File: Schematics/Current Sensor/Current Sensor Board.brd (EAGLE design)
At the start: 67 x 29.2 mm, 4 parts

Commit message: added berbers for current sensor board and flowchart
flow chart is for the main control program.
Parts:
- added C1: (no value), rcl:C050-050X075
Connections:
- net GND: now also C1.2
- net N$3: now also C1.1
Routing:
- net N$3: track 27.1 -> 30.1 mm
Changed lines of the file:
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@@
 <element name="U$3" library="Headers" package="1X2_100MIL" value="1X2HEADER_100MIL" x="2.54" y="15.24" rot="R270"/>
 <element name="IC1" library="v-reg" package="78XXS" value="" x="12.7" y="16.51" rot="R270"/>
+<element name="C1" library="rcl" package="C050-050X075" value="" x="50.8" y="27.94" rot="R180"/>
 </elements>
 <signals>
@@
 <vertex x="0" y="2.54"/>
 </polygon>
+<contactref element="C1" pad="2"/>
 </signal>
 <signal name="N$3">
@@
 <wire x1="44.45" y1="15.24" x2="54.61" y2="25.4" width="0.4064" layer="16"/>
 <wire x1="54.61" y1="25.4" x2="62.23" y2="25.4" width="0.4064" layer="16"/>
+<contactref element="C1" pad="1"/>
+<wire x1="53.34" y1="27.94" x2="53.34" y2="26.67" width="0.4064" layer="16"/>
+<wire x1="53.34" y1="26.67" x2="54.61" y2="25.4" width="0.4064" layer="16"/>
 </signal>
 <signal name="N$1">

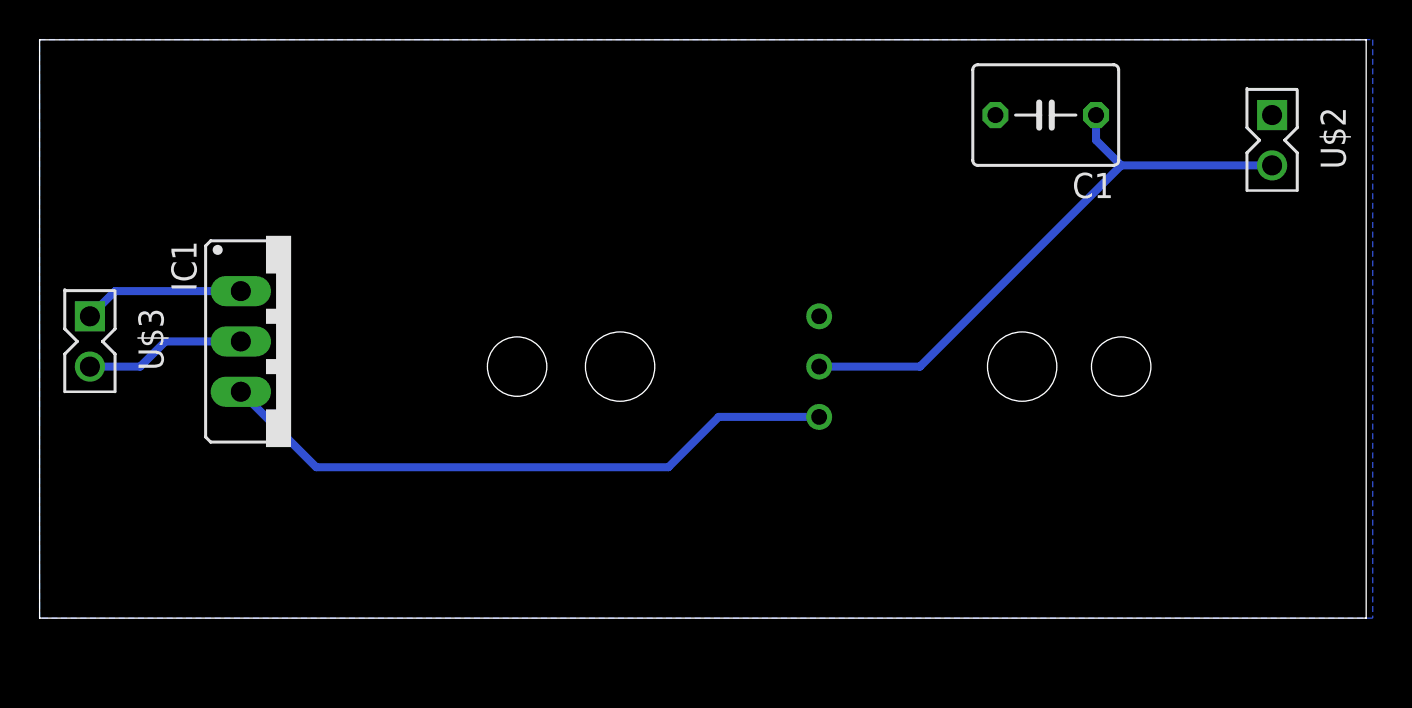
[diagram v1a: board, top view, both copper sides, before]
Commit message: updated documentation and scheamtics
updated current sensor board, and added manual for stepper motor
controller
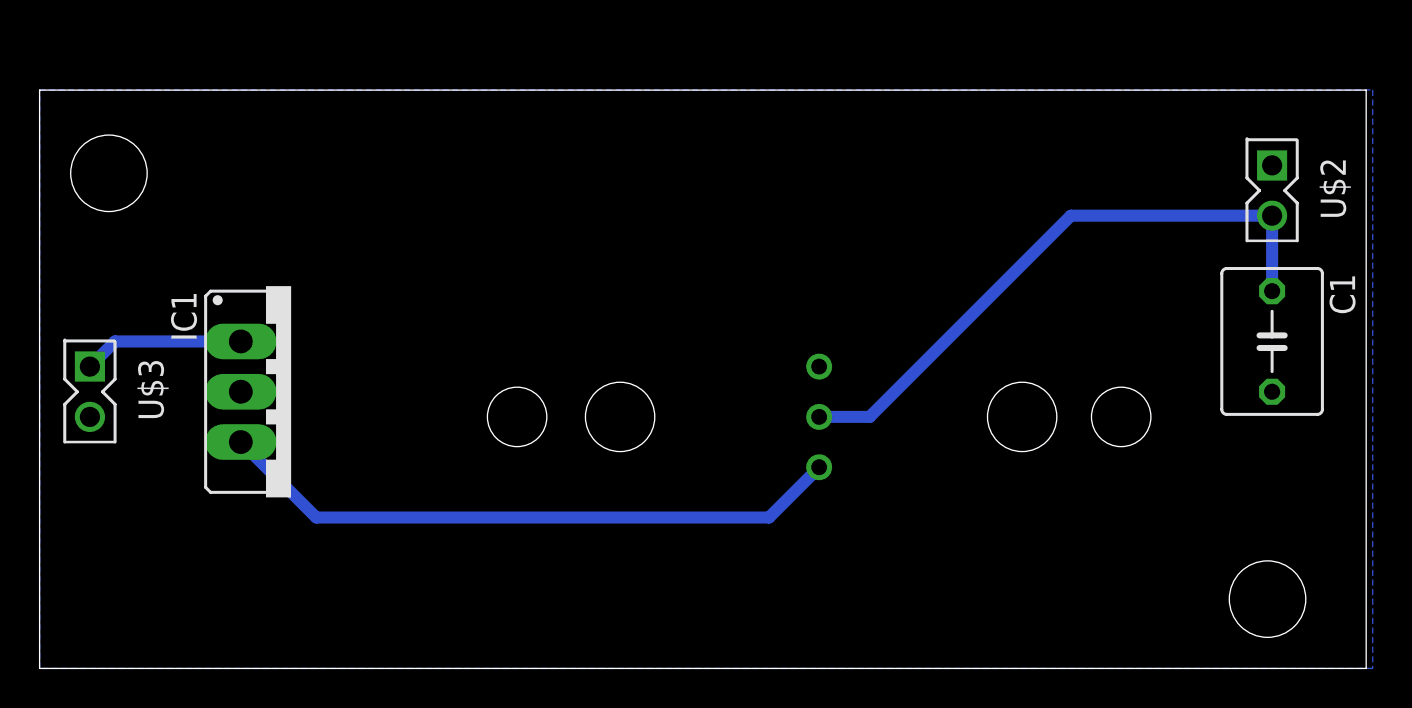
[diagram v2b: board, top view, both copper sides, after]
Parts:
- moved C1 16.2 mm to (62.2, 16.5), turned to 270 degrees
- moved IC1 2.54 mm to (12.7, 14.0)
- moved U$1 2.54 mm to (54.6, 12.7)
- moved U$3 2.54 mm to (2.54, 12.7)
- moved U$2 2.54 mm to (62.2, 22.9)
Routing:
- net GND: track 8.15 -> 0.00 mm
- net N$3: track 30.1 -> 30.9 mm
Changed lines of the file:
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@@
 <setting verticaltext="up"/>
 </settings>
-<grid distance="0.05" unitdist="inch" unit="inch" style="lines" multiple="1" display="yes" altdistance="0.025" altunitdist="inch" altunit="inch"/>
+<grid distance="0.05" unitdist="inch" unit="mil" style="lines" multiple="1" display="yes" altdistance="0.025" altunitdist="inch" altunit="inch"/>
 <layers>
 <layer number="1" name="Top" color="4" fill="1" visible="yes" active="yes"/>
@@
 <layer number="43" name="vRestrict" color="2" fill="10" visible="yes" active="yes"/>
 <layer number="44" name="Drills" color="7" fill="1" visible="no" active="yes"/>
-<layer number="45" name="Holes" color="7" fill="1" visible="no" active="yes"/>
+<layer number="45" name="Holes" color="7" fill="1" visible="yes" active="yes"/>
 <layer number="46" name="Milling" color="3" fill="1" visible="no" active="yes"/>
 <layer number="47" name="Measures" color="7" fill="1" visible="no" active="yes"/>
@@
 <board>
 <plain>
-<wire x1="0" y1="2.54" x2="66.98" y2="2.54" width="0" layer="20"/>
-<wire x1="66.98" y1="2.54" x2="66.98" y2="31.74" width="0" layer="20"/>
-<wire x1="66.98" y1="31.74" x2="0" y2="31.74" width="0" layer="20"/>
-<wire x1="0" y1="31.74" x2="0" y2="2.54" width="0" layer="20"/>
+<wire x1="0" y1="0" x2="66.98" y2="0" width="0" layer="20"/>
+<wire x1="66.98" y1="0" x2="66.98" y2="29.2" width="0" layer="20"/>
+<wire x1="66.98" y1="29.2" x2="0" y2="29.2" width="0" layer="20"/>
+<wire x1="0" y1="29.2" x2="0" y2="0" width="0" layer="20"/>
+<hole x="3.5" y="25" drill="3.8608"/>
+<hole x="62" y="3.5" drill="3.8608"/>
 </plain>
 <attributes>
@@
 </autorouter>
 <elements>
-<element name="U$1" library="Current Sensors" package="CSLA1DJ" value="CSLA1DJ" x="54.61" y="15.24" rot="R180"/>
-<element name="U$2" library="Headers" package="1X2_100MIL" value="1X2HEADER_100MIL" x="62.23" y="25.4" rot="R270"/>
-<element name="U$3" library="Headers" package="1X2_100MIL" value="1X2HEADER_100MIL" x="2.54" y="15.24" rot="R270"/>
-<element name="IC1" library="v-reg" package="78XXS" value="" x="12.7" y="16.51" rot="R270"/>
-<element name="C1" library="rcl" package="C050-050X075" value="" x="50.8" y="27.94" rot="R180"/>
+<element name="U$1" library="Current Sensors" package="CSLA1DJ" value="CSLA1DJ" x="54.61" y="12.7" rot="R180"/>
+<element name="U$2" library="Headers" package="1X2_100MIL" value="1X2HEADER_100MIL" x="62.23" y="22.86" rot="R270"/>
+<element name="U$3" library="Headers" package="1X2_100MIL" value="1X2HEADER_100MIL" x="2.54" y="12.7" rot="R270"/>
+<element name="IC1" library="v-reg" package="78XXS" value="" x="12.7" y="13.97" rot="R270"/>
+<element name="C1" library="rcl" package="C050-050X075" value="" x="62.23" y="16.51" rot="R270"/>
 </elements>
 <signals>
@@
 <contactref element="U$1" pad="V+"/>
 <contactref element="IC1" pad="OUT"/>
-<wire x1="10.16" y1="13.97" x2="13.97" y2="10.16" width="0.4064" layer="16"/>
-<wire x1="13.97" y1="10.16" x2="31.75" y2="10.16" width="0.4064" layer="16"/>
-<wire x1="31.75" y1="10.16" x2="34.29" y2="12.7" width="0.4064" layer="16"/>
-<wire x1="34.29" y1="12.7" x2="39.36" y2="12.7" width="0.4064" layer="16"/>
+<wire x1="10.16" y1="11.43" x2="13.97" y2="7.62" width="0.6096" layer="16"/>
+<wire x1="13.97" y1="7.62" x2="36.83" y2="7.62" width="0.6096" layer="16"/>
+<wire x1="36.83" y1="7.62" x2="39.36" y2="10.15" width="0.6096" layer="16"/>
+<wire x1="39.36" y1="10.15" x2="39.36" y2="10.16" width="0.6096" layer="16"/>
 </signal>
 <signal name="GND">
@@
 <contactref element="U$2" pad="1"/>
 <contactref element="IC1" pad="GND"/>
-<wire x1="2.54" y1="15.24" x2="5.08" y2="15.24" width="0.4064" layer="16"/>
-<wire x1="5.08" y1="15.24" x2="6.35" y2="16.51" width="0.4064" layer="16"/>
-<wire x1="6.35" y1="16.51" x2="10.16" y2="16.51" width="0.4064" layer="16"/>
 <polygon width="0.4064" layer="16" isolate="0.6096">
-<vertex x="0" y="31.75"/>
-<vertex x="67.31" y="31.75"/>
-<vertex x="67.31" y="2.54"/>
-<vertex x="0" y="2.54"/>
+<vertex x="0" y="29.21"/>
+<vertex x="67.31" y="29.21"/>
+<vertex x="67.31" y="0"/>
+<vertex x="0" y="0"/>
 </polygon>
 <contactref element="C1" pad="2"/>
@@
 <contactref element="U$1" pad="V0"/>
 <contactref element="U$2" pad="2"/>
-<wire x1="39.36" y1="15.24" x2="44.45" y2="15.24" width="0.4064" layer="16"/>
-<wire x1="44.45" y1="15.24" x2="54.61" y2="25.4" width="0.4064" layer="16"/>
-<wire x1="54.61" y1="25.4" x2="62.23" y2="25.4" width="0.4064" layer="16"/>
 <contactref element="C1" pad="1"/>
-<wire x1="53.34" y1="27.94" x2="53.34" y2="26.67" width="0.4064" layer="16"/>
-<wire x1="53.34" y1="26.67" x2="54.61" y2="25.4" width="0.4064" layer="16"/>
+<wire x1="52.07" y1="22.86" x2="62.23" y2="22.86" width="0.6096" layer="16"/>
+<wire x1="39.36" y1="12.7" x2="41.91" y2="12.7" width="0.6096" layer="16"/>
+<wire x1="41.91" y1="12.7" x2="52.07" y2="22.86" width="0.6096" layer="16"/>
+<wire x1="62.23" y1="19.05" x2="62.23" y2="22.86" width="0.6096" layer="16"/>
 </signal>
 <signal name="N$1">
 <contactref element="U$3" pad="1"/>
 <contactref element="IC1" pad="IN"/>
-<wire x1="2.54" y1="17.78" x2="3.81" y2="19.05" width="0.4064" layer="16"/>
-<wire x1="3.81" y1="19.05" x2="10.16" y2="19.05" width="0.4064" layer="16"/>
+<wire x1="2.54" y1="15.24" x2="3.81" y2="16.51" width="0.6096" layer="16"/>
+<wire x1="3.81" y1="16.51" x2="10.16" y2="16.51" width="0.6096" layer="16"/>
 </signal>
 </signals>
